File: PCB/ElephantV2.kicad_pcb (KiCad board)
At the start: 2 copper layers, 58 parts

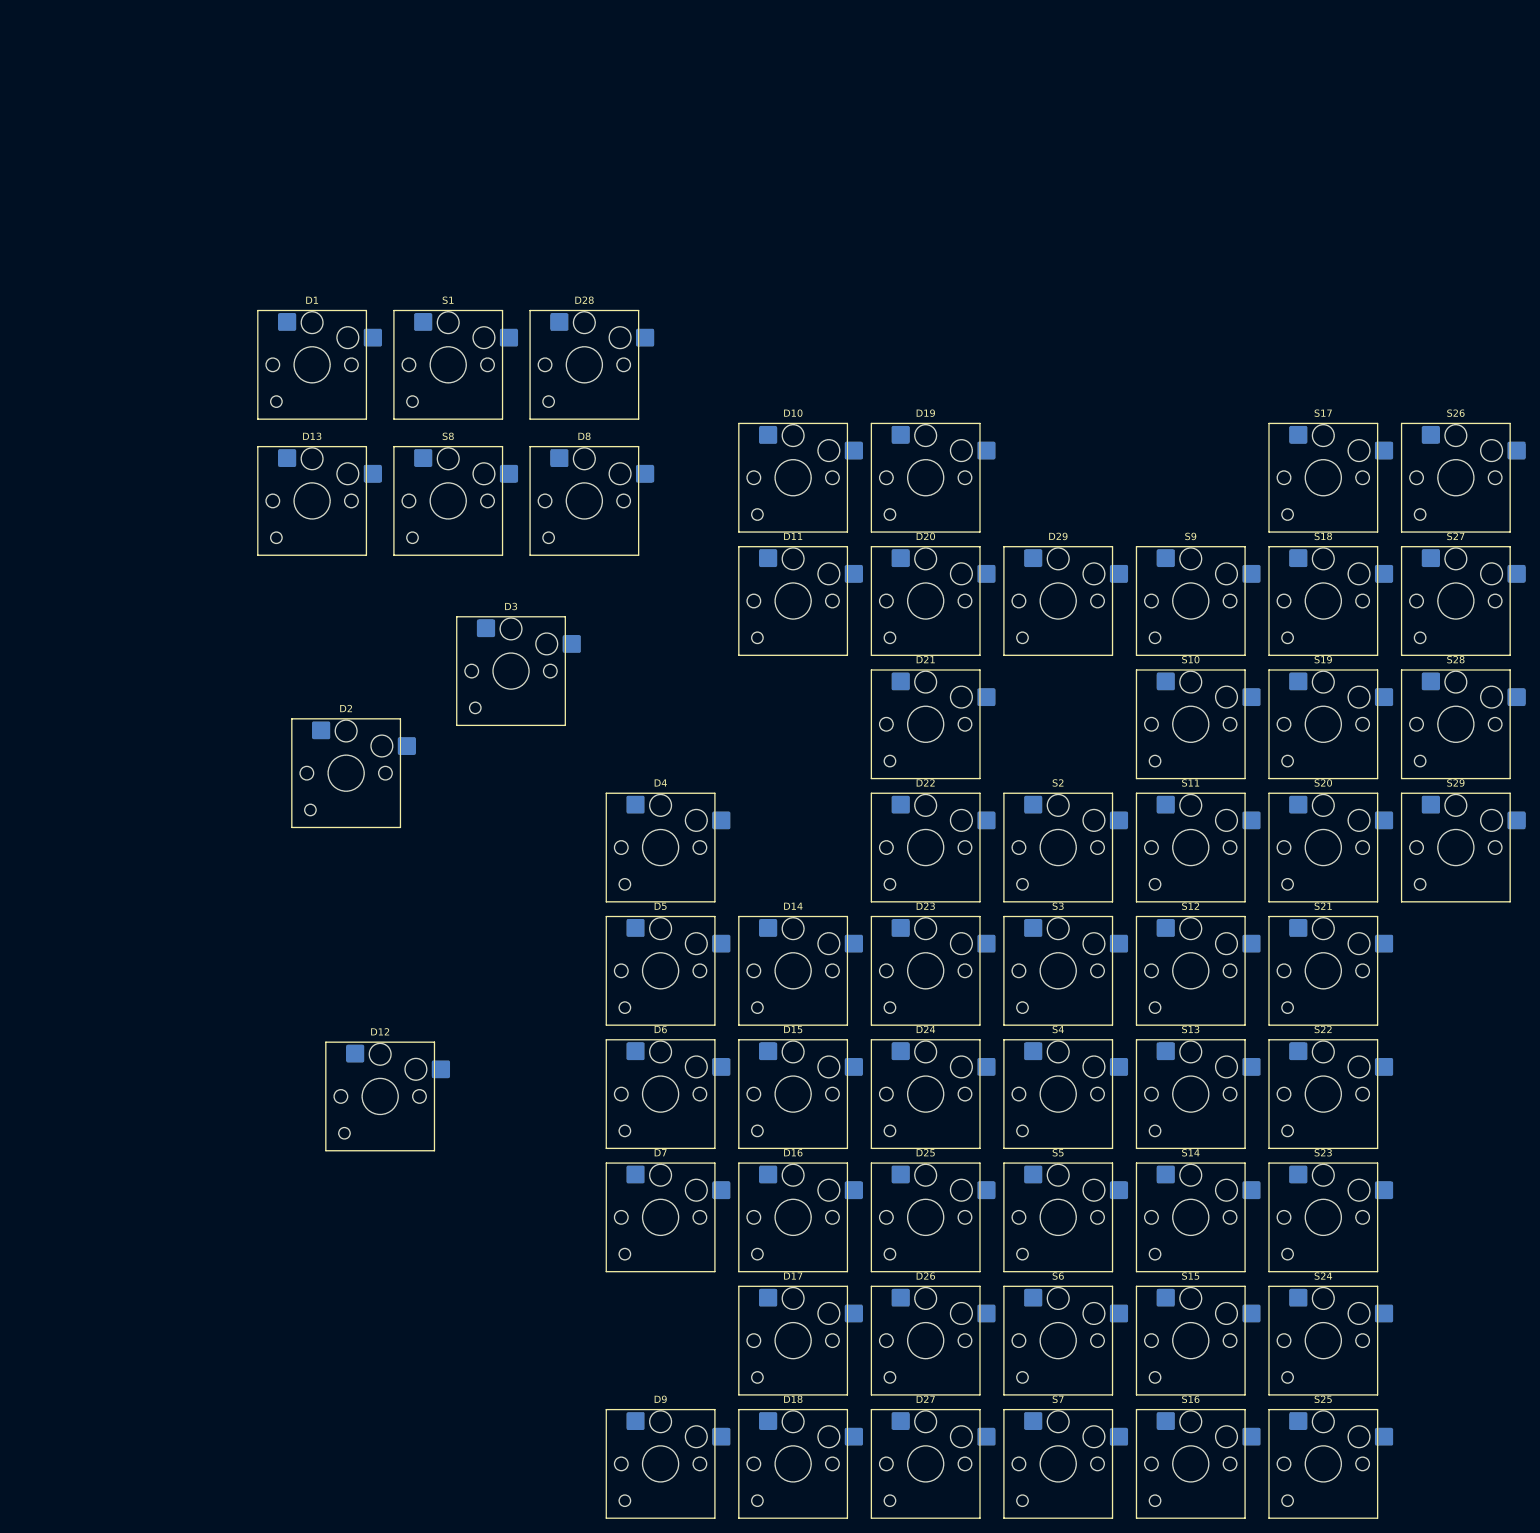
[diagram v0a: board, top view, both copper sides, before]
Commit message: Improved the layout of the keyboard in the schematic and pcb. Updated the readmefile
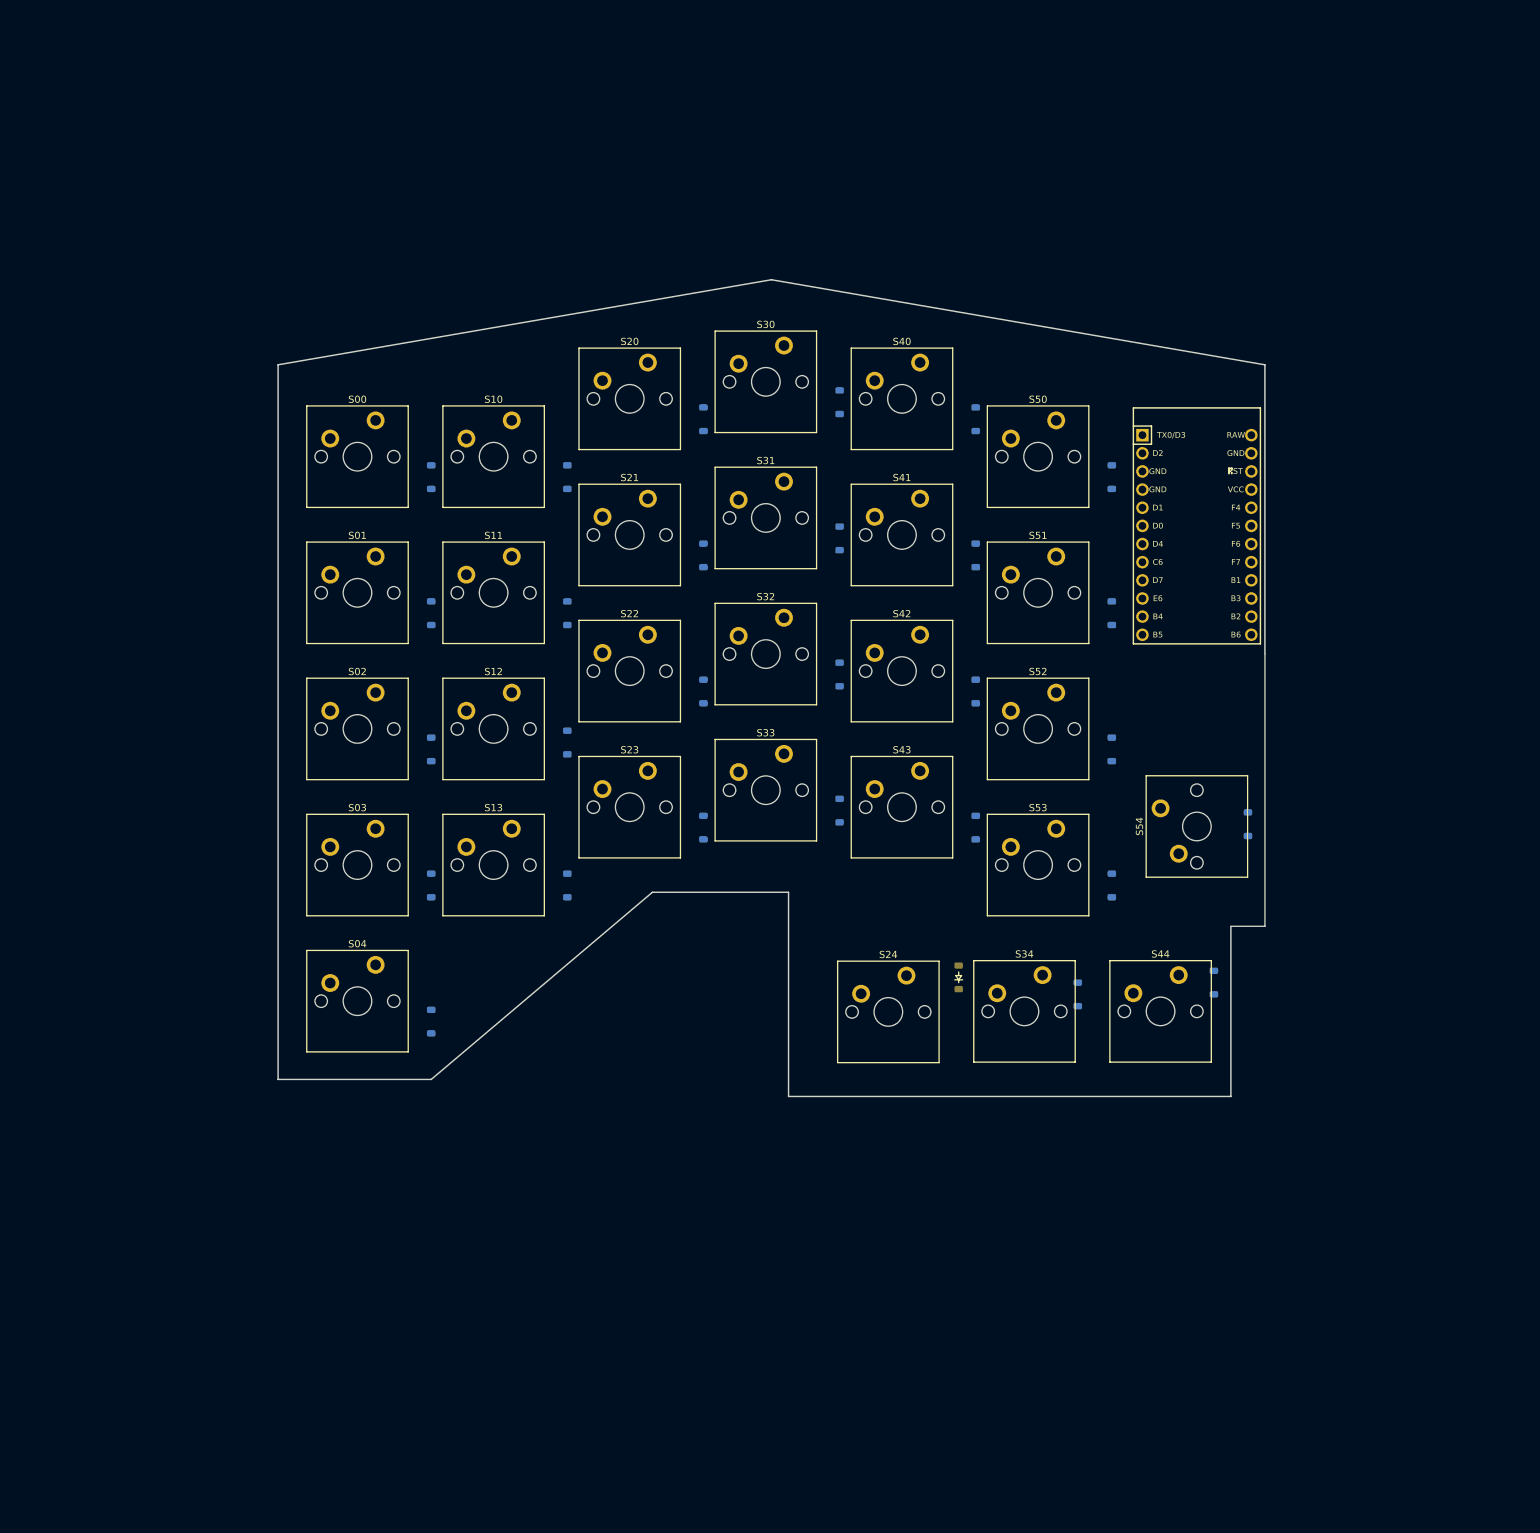
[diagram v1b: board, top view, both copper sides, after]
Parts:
- removed D1, D14, D15, D16, D17, D18, D19, D2, D25, D26, D27, D28, D29, D3, D4, D5, D6, D7, D8, D9: Diode, PCM_Switch_Keyboard_Hotswap_Kailh:SW_Hotswap_Kailh_Choc_V1V2_1.00u
- removed S1, S14, S15, S16, S17, S18, S19, S2, S25, S26, S27, S28, S29, S3, S4, S5, S6, S7, S8, S9: Keyswitch, PCM_Switch_Keyboard_Hotswap_Kailh:SW_Hotswap_Kailh_Choc_V1V2_1.00u
- added D00: Diode, ScottoKeebs_Components:Diode_SOD-123, B.Cu at (38.1, 37.1)
- added D01: Diode, ScottoKeebs_Components:Diode_SOD-123, B.Cu at (38.1, 56.2)
- added D02: Diode, ScottoKeebs_Components:Diode_SOD-123, B.Cu at (38.1, 75.2)
- added D03: Diode, ScottoKeebs_Components:Diode_SOD-123, B.Cu at (38.1, 94.3)
- added D04: Diode, ScottoKeebs_Components:Diode_SOD-123, B.Cu at (38.1, 113.3)
- added D30: Diode, ScottoKeebs_Components:Diode_SOD-123, B.Cu at (95.2, 26.7)
- added D31: Diode, ScottoKeebs_Components:Diode_SOD-123, B.Cu at (95.2, 45.7)
- added D32: Diode, ScottoKeebs_Components:Diode_SOD-123, B.Cu at (95.2, 64.8)
- added D33: Diode, ScottoKeebs_Components:Diode_SOD-123, B.Cu at (95.2, 83.8)
- added D34: Diode, ScottoKeebs_Components:Diode_SOD-123, B.Cu at (128.6, 109.5)
- added D40: Diode, ScottoKeebs_Components:Diode_SOD-123, B.Cu at (114.3, 29.1)
- added D41: Diode, ScottoKeebs_Components:Diode_SOD-123, B.Cu at (114.3, 48.1)
- added D42: Diode, ScottoKeebs_Components:Diode_SOD-123, B.Cu at (114.3, 67.2)
- added D43: Diode, ScottoKeebs_Components:Diode_SOD-123, B.Cu at (114.3, 86.2)
- added D44: Diode, ScottoKeebs_Components:Diode_SOD-123, B.Cu at (147.6, 107.9)
- added D50: Diode, ScottoKeebs_Components:Diode_SOD-123, B.Cu at (133.3, 37.1)
- added D51: Diode, ScottoKeebs_Components:Diode_SOD-123, B.Cu at (133.3, 56.2)
- added D52: Diode, ScottoKeebs_Components:Diode_SOD-123, B.Cu at (133.3, 75.2)
- added D53: Diode, ScottoKeebs_Components:Diode_SOD-123, B.Cu at (133.3, 94.3)
- added D54: Diode, ScottoKeebs_Components:Diode_SOD-123, B.Cu at (152.4, 85.7)
- added S00: Keyswitch, ScottoKeebs_MX:MX_PCB_1.00u, F.Cu at (27.8, 34.3)
- added S01: Keyswitch, ScottoKeebs_MX:MX_PCB_1.00u, F.Cu at (27.8, 53.3)
- added S02: Keyswitch, ScottoKeebs_MX:MX_PCB_1.00u, F.Cu at (27.8, 72.4)
- added S03: Keyswitch, ScottoKeebs_MX:MX_PCB_1.00u, F.Cu at (27.8, 91.4)
- added S04: Keyswitch, ScottoKeebs_MX:MX_PCB_1.00u, F.Cu at (27.8, 110.5)
- added S30: Keyswitch, ScottoKeebs_MX:MX_PCB_1.00u, F.Cu at (84.9, 23.8)
- added S31: Keyswitch, ScottoKeebs_MX:MX_PCB_1.00u, F.Cu at (84.9, 42.9)
- added S32: Keyswitch, ScottoKeebs_MX:MX_PCB_1.00u, F.Cu at (84.9, 61.9)
- added S33: Keyswitch, ScottoKeebs_MX:MX_PCB_1.00u, F.Cu at (84.9, 81.0)
- added S34: Keyswitch, ScottoKeebs_MX:MX_PCB_1.00u, F.Cu at (121.1, 111.9)
- added S40: Keyswitch, ScottoKeebs_MX:MX_PCB_1.00u, F.Cu at (104.0, 26.2)
- added S41: Keyswitch, ScottoKeebs_MX:MX_PCB_1.00u, F.Cu at (104.0, 45.2)
- added S42: Keyswitch, ScottoKeebs_MX:MX_PCB_1.00u, F.Cu at (104.0, 64.3)
- added S43: Keyswitch, ScottoKeebs_MX:MX_PCB_1.00u, F.Cu at (104.0, 83.3)
- added S44: Keyswitch, ScottoKeebs_MX:MX_PCB_1.00u, F.Cu at (140.2, 111.9)
- added S50: Keyswitch, ScottoKeebs_MX:MX_PCB_1.00u, F.Cu at (123.0, 34.3)
- added S51: Keyswitch, ScottoKeebs_MX:MX_PCB_1.00u, F.Cu at (123.0, 53.3)
- added S52: Keyswitch, ScottoKeebs_MX:MX_PCB_1.00u, F.Cu at (123.0, 72.4)
- added S53: Keyswitch, ScottoKeebs_MX:MX_PCB_1.00u, F.Cu at (123.0, 91.4)
- added S54: Keyswitch, ScottoKeebs_MX:MX_PCB_1.50u, F.Cu at (145.3, 86.0)
- added U1: Nice_Nano_V2, ScottoKeebs_MCU:Arduino_Pro_Micro, F.Cu at (145.3, 45.2)
- D10, D11, D12, D13, D20, D21, D22, D23: footprint PCM_Switch_Keyboard_Hotswap_Kailh:SW_Hotswap_Kailh_Choc_V1V2_1.00u -> ScottoKeebs_Components:Diode_SOD-123; moved to B.Cu
- D24: footprint PCM_Switch_Keyboard_Hotswap_Kailh:SW_Hotswap_Kailh_Choc_V1V2_1.00u -> ScottoKeebs_Components:Diode_SOD-123
- S10, S11, S12, S13, S20, S21, S22, S23, S24: footprint PCM_Switch_Keyboard_Hotswap_Kailh:SW_Hotswap_Kailh_Choc_V1V2_1.00u -> ScottoKeebs_MX:MX_PCB_1.00u
- moved S20 115.6 mm to (65.9, 26.2)
- moved S21 114.6 mm to (65.9, 45.2)
- moved S22 113.7 mm to (65.9, 64.3)
- moved S23 112.8 mm to (65.9, 83.3)
- moved S10 104.5 mm to (46.8, 34.3)
- moved S11 103.9 mm to (46.8, 53.3)
- moved S12 103.3 mm to (46.8, 72.4)
- moved S13 102.7 mm to (46.8, 91.4)
- moved S24 76.3 mm to (102.1, 112.0)
- moved D13 64.6 mm to (57.1, 94.3), turned to 90 degrees
- moved D12 56.0 mm to (57.1, 74.3), turned to 90 degrees
- moved D20 40.2 mm to (76.2, 29.1), turned to 90 degrees
- moved D21 39.1 mm to (76.2, 48.1), turned to 90 degrees
- moved D22 38.0 mm to (76.2, 67.2), turned to 90 degrees
- moved D23 37.0 mm to (76.2, 86.2), turned to 90 degrees
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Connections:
- D10 pad 1: R2 -> R0
- D12 pad 1: R0 -> R2
- D21 pad 1: R3 -> R1
- D23 pad 1: R1 -> R3
- D24 pad 1: R0 -> R4
- S10 pad 1: C2 -> C1
- S11 pad 1: C2 -> C1
- S12 pad 1: C2 -> C1
- S13 pad 1: C3 -> C1
- S20 pad 1: C4 -> C2
- S21 pad 1: C5 -> C2
- S22 pad 1: C5 -> C2
- S23 pad 1: C5 -> C2
- S24 pad 1: C5 -> C2
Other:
- board outline added: 138.1 x 114.3 mm

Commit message: Made it choc changed the layout to be 3x6_4
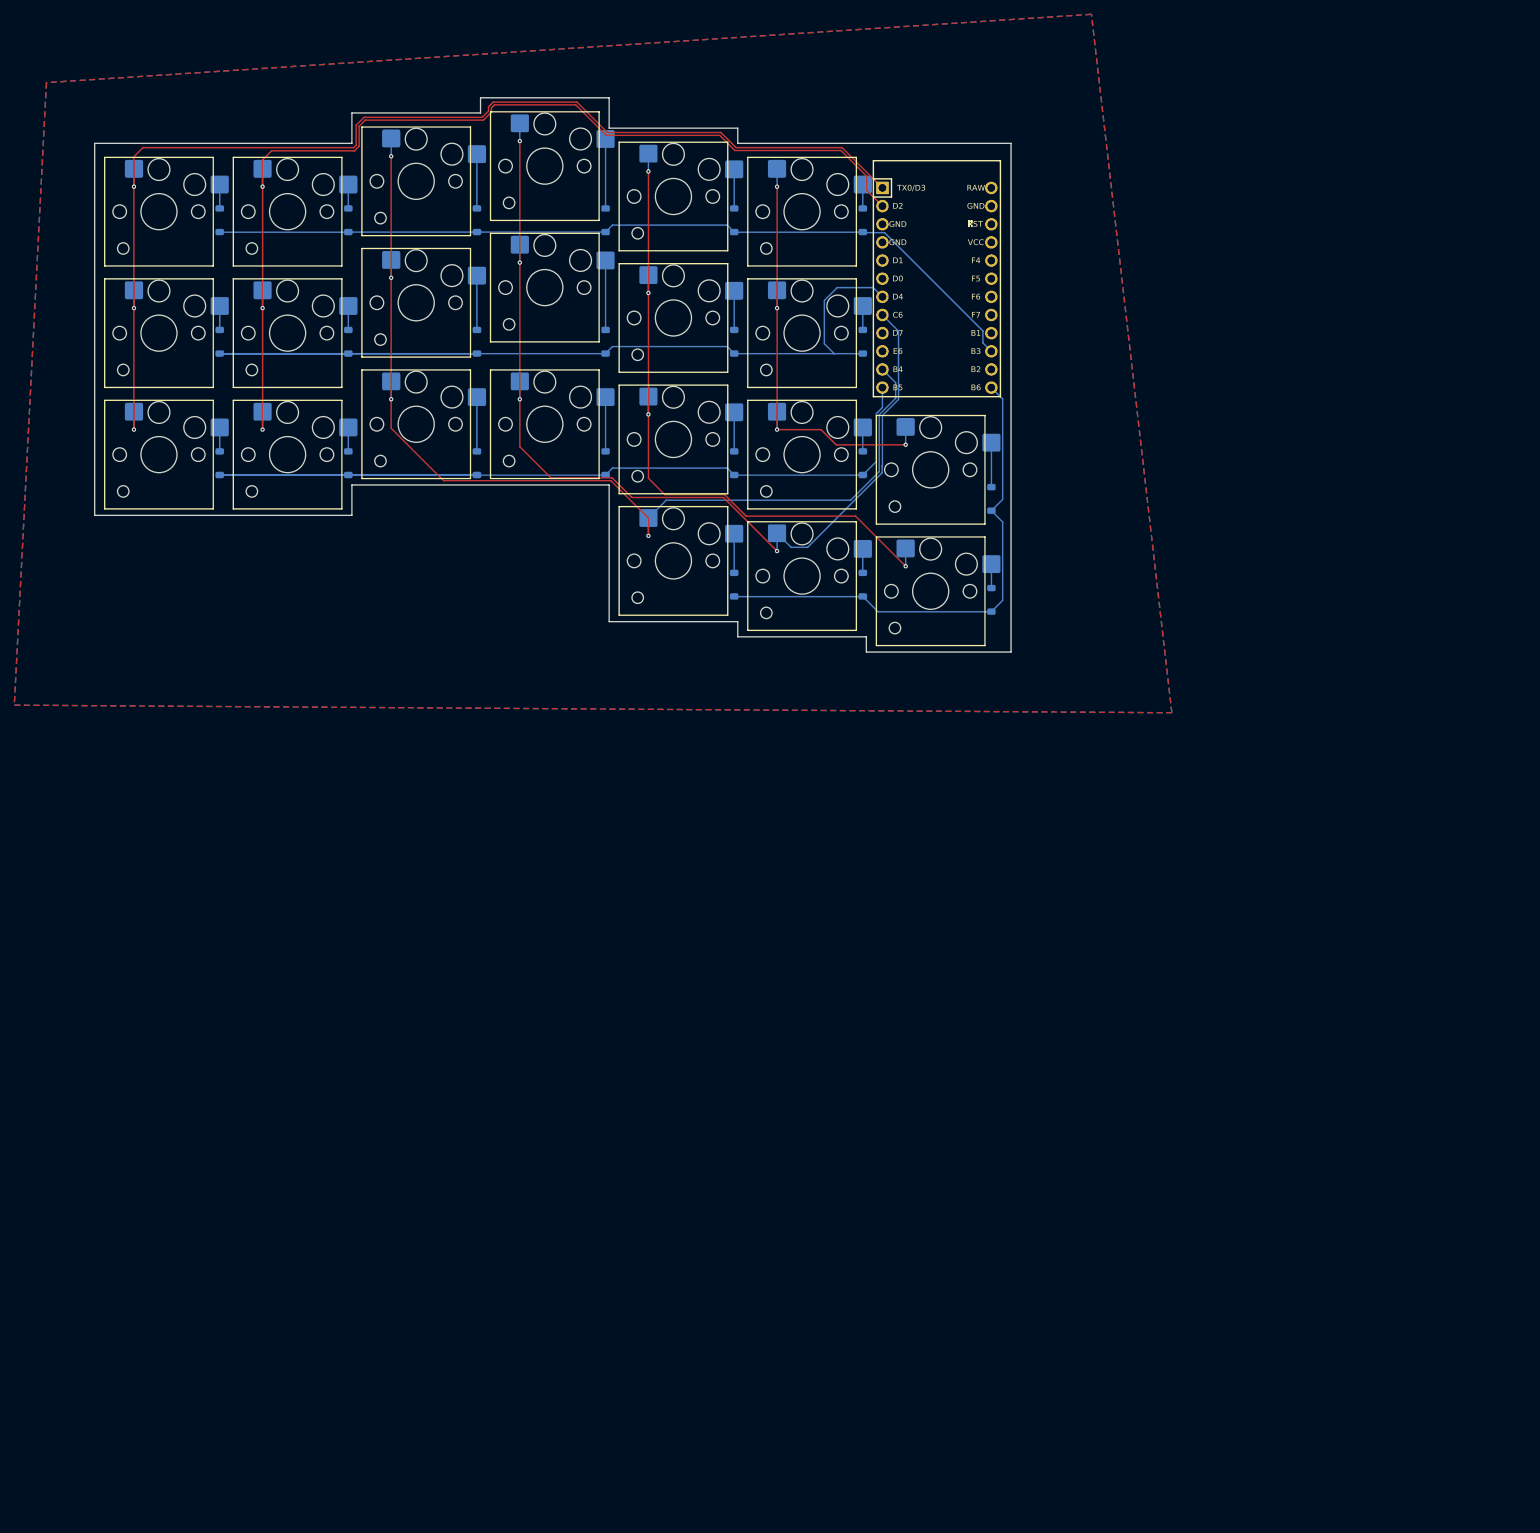
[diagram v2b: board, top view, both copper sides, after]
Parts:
- removed D03, D04, D13, D24, D34, D44, D54: Diode, ScottoKeebs_Components:Diode_SOD-123
- removed S03, S04, S13, S24, S34, S44: Keyswitch, ScottoKeebs_MX:MX_PCB_1.00u
- removed S54: Keyswitch, ScottoKeebs_MX:MX_PCB_1.50u
- S00, S01, S02, S10, S11, S12, S20, S21, S22, S23, S30, S31, S32, S33, S40, S41, S42, S43, S50, S51, S52, S53: footprint ScottoKeebs_MX:MX_PCB_1.00u -> ScottoKeebs_Hotswap:Hotswap_Choc_V1V2_1.00u
- moved S53 57.3 mm to (108.0, 36.1)
- moved D53 56.7 mm to (116.5, 40.2)
- moved D52 53.1 mm to (98.5, 35.2)
- moved D51 51.6 mm to (98.5, 18.2)
- moved S52 50.6 mm to (90.0, 34.0)
- moved U1 50.2 mm to (108.9, 10.7)
- moved D50 50.1 mm to (98.5, 1.20)
- moved D02 49.8 mm to (8.50, 35.2)
- moved D12 49.7 mm to (26.5, 35.2)
- moved S51 49.1 mm to (90.0, 17.0)
- moved D11 48.8 mm to (26.5, 18.2)
- moved D01 48.2 mm to (8.50, 18.2)
- moved S12 48.0 mm to (18.0, 34.0)
- moved S50 47.6 mm to (90.0, 0.00)
- moved S02 47.4 mm to (0.00, 34.0)
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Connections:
- U1 pad 1: C1 -> C0
- U1 pad 11: R1 -> C2
- U1 pad 2: C0 -> C1
- U1 pad 23: unconnected-(U1-GND-Pad23) -> GND
- U1 pad 3: unconnected-(U1-GND-Pad3) -> GND
- U1 pad 4: unconnected-(U1-GND-Pad4) -> GND
- U1 pad 5: C2 -> C5
- U1 pad 6: C3 -> C4
- U1 pad 7: C4 -> R1
- U1 pad 8: C5 -> C3
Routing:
- net R1: track 0.00 -> 162.2 mm
- net C0: track 0.00 -> 160.6 mm, vias 0 -> 3
- net R2: track 0.00 -> 158.2 mm
- net C1: track 0.00 -> 144.2 mm, vias 0 -> 3
- net C2: track 0.00 -> 142.8 mm, vias 0 -> 4
- net C3: track 0.00 -> 138.6 mm, vias 0 -> 4
- net R0: track 0.00 -> 116.7 mm
- net C4: track 0.00 -> 94.0 mm, vias 0 -> 4
- net R3: track 0.00 -> 70.9 mm
- net C5: track 0.00 -> 62.9 mm, vias 0 -> 4
- net Net-(D31-A): track 0.00 -> 9.73 mm
- net Net-(D30-A): track 0.00 -> 9.73 mm
- net Net-(D21-A): track 0.00 -> 7.60 mm
- net Net-(D20-A): track 0.00 -> 7.60 mm
- net Net-(D32-A): track 0.00 -> 7.60 mm
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- added copper zone on B.Cu, net GND
- added copper zone on F.Cu, net GND
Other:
- board size 138.1 x 114.3 mm -> 128.2 x 77.6 mm
